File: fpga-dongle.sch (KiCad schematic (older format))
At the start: 82 parts, among them P1 right, P2 left, U1 W25Q16BVSSIG(SOIC-8_208mil), U2 SY8009AAAC(SOT23-5), U3 SY8009AAAC(SOT23-5), U4 ICE40HX1K-VQ100(VQFP100), U5 AS4C16M16S

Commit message: Assigned componets, first partial place
Signed-off-by: Martin Ribelotta <martinribelotta@gmail.com>
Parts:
- 3.3V_E1, RxD_E1, TxD_E1: footprint OLIMEX_Jumpers-FP:SJ -> OLIMEX:SJ
- BUT1, RESET1: footprint OLIMEX_Buttons-FP:T1107A(6x3,8x2,5MM) -> OLIMEX:T1107A(6x3,8x2,5MM)
- C1, C10, C2, C7, C8, C9: footprint OLIMEX_RLC-FP:C_0603_5MIL_DWS -> OLIMEX:C_0805_5MIL_DWS
- C11, C12, C13, C14, C15, C16, C17, C18, C19, C20, C21, C22, C23, C24, C25, C3, C4: footprint OLIMEX_RLC-FP:C_0402_5MIL_DWS -> OLIMEX:C_0805_5MIL_DWS
- C26, C27, C28, C29, C30, C31, C32, C33: footprint Capacitors_SMD:C_0805 -> OLIMEX:C_0805_5MIL_DWS
- C5, C6: footprint OLIMEX_RLC-FP:C_0805_5MIL_DWS -> OLIMEX:C_0805_5MIL_DWS
- CDone1, LED1, PWRLED1: footprint OLIMEX_LEDs-FP:LED_0603_KA -> LEDs:LED-0805
- CR1: footprint OLIMEX_Crystal-FP:Oscillator_7.0x5.0mm -> OLIMEX:Oscillator_7.0x5.0mm
- D1: footprint OLIMEX_Diodes-FP:DO214AA -> OLIMEX:DO214AA
- D2: footprint OLIMEX_Diodes-FP:SOD-123_1C-2A_KA -> OLIMEX:SOD-123_1C-2A_KA
- FUSE1: footprint OLIMEX_Devices-FP:FUSE-5025 -> OLIMEX:FUSE-5025
- GND1: footprint OLIMEX_Other-FP:TEST_PAD40x70_SQUARE -> OLIMEX:TEST_PAD40x70_SQUARE
- L1, L2: footprint OLIMEX_RLC-FP:CD32 -> OLIMEX:CD32
- P1, P2: footprint (none) -> Pin_Headers:Pin_Header_Straight_2x20
- P3: renamed from P?; footprint (none) -> Pin_Headers:Pin_Header_Straight_2x10
- PGM1: footprint OLIMEX_Connectors-FP:UEXT_ML10 -> OLIMEX:UEXT_ML10
- PWR1: footprint OLIMEX_Connectors-FP:PWRJ-2mm(YDJ-1136) -> OLIMEX:PWRJ-2mm(YDJ-1136)
- R1, R17, R18, R19, R2, R20, R21, R22, R23, R24, R3, R4: renamed from R?; footprint OLIMEX_RLC-FP:R_0402_5MIL_DWS -> Resistors_SMD:R_0805
- R10, R11, R12, R13, R14, R15, R16, R5, R6, R7, R8, R9: footprint OLIMEX_RLC-FP:R_0402_5MIL_DWS -> Resistors_SMD:R_0805
- U1: footprint OLIMEX_IC-FP:SO-8_208mil -> OLIMEX:SO-8_208mil
- U2, U3: footprint OLIMEX_IC-FP:SOT-23-5 -> OLIMEX:SOT-23-5
- U4: footprint OLIMEX_IC-FP:VQFP100_Pitch-0.5mm_Dimensions-16.00x16.00x1.20mm -> OLIMEX:VQFP100_Pitch-0.5mm_Dimensions-16.00x16.00x1.20mm
- U5: footprint footprints:TSOP_II_54 -> OLIMEX:SOIC-54

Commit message: First 144LQFP version. To be revised
Signed-off-by: Martin Ribelotta <martinribelotta@gmail.com>
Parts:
- removed 3.3V_E1, RxD_E1, TxD_E1: Opened, OLIMEX:SJ, symbol SJ
- removed BUT1, RESET1: T1107A(6x3,8x2,5MM), OLIMEX:T1107A(6x3,8x2,5MM), symbol T1107A(6x3,8x2,5MM)
- removed C10, C9: 22uF/6.3V/0603, OLIMEX:C_0805_5MIL_DWS, symbol C_Small
- removed C15: 100nF, OLIMEX:C_0805_5MIL_DWS, symbol C_Small
- removed C26: 100p, OLIMEX:C_0805_5MIL_DWS, symbol Csmall
- removed C27, C28, C29, C30, C31, C32, C33: 100n, OLIMEX:C_0805_5MIL_DWS, symbol Csmall
- removed D1: SMBJ6.0A, OLIMEX:DO214AA, symbol SMBJ6.0A
- removed FUSE1: NA(5025), OLIMEX:FUSE-5025, symbol FSMD035
- removed GND1: TESTPAD, OLIMEX:TEST_PAD40x70_SQUARE, symbol TESTPAD
- removed L1, L2: 2.2uH/1.5A/DCR<0.1R/CD32, OLIMEX:CD32, symbol L
- removed P3: CONN_01X20, Pin_Headers:Pin_Header_Straight_2x10, symbol CONN_01X20
- removed PGM1: BH10S, OLIMEX:UEXT_ML10, symbol BH10S
- removed PWR1: PWRJ-2mm(YDJ-1136), OLIMEX:PWRJ-2mm(YDJ-1136), symbol PWR-JAKPWR_JACK_UNI_MILLING
- removed R10: NA(22R), Resistors_SMD:R_0805, symbol R
- removed R17, R18, R19, R20, R21, R22, R23, R24: 0, Resistors_SMD:R_0805, symbol R
- removed R5, R7, R8: 4.99k/1%, Resistors_SMD:R_0805, symbol R
- removed R6: 1.1k/1%, Resistors_SMD:R_0805, symbol R
- removed U2, U3: SY8009AAAC(SOT23-5), OLIMEX:SOT-23-5, symbol SY8009AAAC(SOT23-5)
- removed U4: ICE40HX1K-VQ100(VQFP100), OLIMEX:VQFP100_Pitch-0.5mm_Dimensions-16.00x16.00x1.20mm, symbol ICE40HX1K-VQ100(VQFP100)
- added C19, C23: 100nF, OLIMEX:C_0805_5MIL_DWS, symbol C_Small
- added C25, C26, C27, C28, C29, C30, C31, C32: 100nF, symbol C_Small
- added D1: SMBJ6.0A, symbol TVS
- added F1: 1A, symbol F_Small
- added L1, L2: 2.2uH, symbol L_Small
- added P1: USB_PWR, symbol USB_OTG
- added P2: PGM, symbol CONN_02X04
- added R12: 100R, Resistors_SMD:R_0805, symbol R
- added RESET1, SW1: T1107A(6x3,8x2,5MM), symbol SW_PUSH
- added U2: sc189(Z) 3.3v, symbol sc189x
- added U3: sc189(C) 1.2v, symbol sc189x
- added U4: iCE40-HX4K-TQ144, symbol iCE40-HX4K-TQ144
- C11: value 100nF -> 10uF
- C8: renamed from C7; value 22uF/6.3V/0603 -> 10uF/6.3V/0603
- C9: renamed from C8; value 22uF/6.3V/0603 -> 10uF/6.3V/0603
- CR1: value Oscillator-100MHZ_TXC-7W -> Oscillator-50MHZ_TXC-7W
- renumbered C3 to C1, C23 to C10, C25 to C15, C1 to C2, C2 to C3, C19 to C6, C6 to C7, P1 to P3, P2 to P4, R15 to R1, R12 to R10, R13 to R11, R1 to R2, R2 to R3, R3 to R4, R4 to R5, R16 to R6, R9 to R7, R11 to R8, R14 to R9
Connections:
- net labels added: FPGA_IO_BANK1_0, FPGA_IO_BANK1_1, FPGA_IO_BANK1_10, FPGA_IO_BANK1_11, FPGA_IO_BANK1_12, FPGA_IO_BANK1_13, FPGA_IO_BANK1_14, FPGA_IO_BANK1_15, FPGA_IO_BANK1_16, FPGA_IO_BANK1_17, FPGA_IO_BANK1_18, FPGA_IO_BANK1_19, FPGA_IO_BANK1_2, FPGA_IO_BANK1_20, FPGA_IO_BANK1_21, FPGA_IO_BANK1_22, FPGA_IO_BANK1_23, FPGA_IO_BANK1_3, FPGA_IO_BANK1_4, FPGA_IO_BANK1_5, FPGA_IO_BANK1_6, FPGA_IO_BANK1_7, FPGA_IO_BANK1_8, FPGA_IO_BANK1_9, FPGA_IO_BANK2_0, FPGA_IO_BANK2_1, FPGA_IO_BANK2_10, FPGA_IO_BANK2_11, FPGA_IO_BANK2_12, FPGA_IO_BANK2_13, FPGA_IO_BANK2_14, FPGA_IO_BANK2_15, FPGA_IO_BANK2_16, FPGA_IO_BANK2_17, FPGA_IO_BANK2_18, FPGA_IO_BANK2_19, FPGA_IO_BANK2_2, FPGA_IO_BANK2_20, FPGA_IO_BANK2_21, FPGA_IO_BANK2_22, FPGA_IO_BANK2_23, FPGA_IO_BANK2_24, FPGA_IO_BANK2_25, FPGA_IO_BANK2_26, FPGA_IO_BANK2_27, FPGA_IO_BANK2_3, FPGA_IO_BANK2_4, FPGA_IO_BANK2_5, FPGA_IO_BANK2_6, FPGA_IO_BANK2_7, FPGA_IO_BANK2_8, FPGA_IO_BANK2_9, RxD, SPI_CLK, SPI_CS, TxD
- net labels removed: LCD_EN, PIO2_1, PIO2_2/I2C_SDA, PIO2_3/I2C_SCL, PIO2_4/SPI_CS, PIO2_5/SPI_MOSI, PIO2_6/SPI_MISO, PIO2_7/SPI_CLK, PIO2_8/RxD, PIO2_9/TxD, PIO3_10A, PIO3_10B, PIO3_12A, PIO3_12B, PIO3_1A, PIO3_1B, PIO3_2A, PIO3_2B, PIO3_3A, PIO3_3B, PIO3_5A, PIO3_5B, PIO3_6A, PIO3_6B, PIO3_7B, PIO3_8A, PIO3_8B
- wire segments 301 -> 195
- no-connect marks 4 -> 9
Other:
- note added: "EDU-CIAA Link"
- note added: "External IO (52 GPIO)"
- note added: "FPGA SDRAM IO and FPGA CIAA Link"
- note added: "GBIN0 as CLK"
- note added: "GBIN1 as input\nor global reset"
- note added: "L: 1.5A\nDCR<0.1R\nCD32"
- note added: "SDRAM Memory"
- note removed: "+5VDC ONLY!!!"
- note removed: "GFC was read up to the Board's part at 12.02.2016!"
- note removed: "Ra"
- note removed: "Rb"
- note removed: "Rc"
- note removed: "Rd"
- note removed: "Vout=0.6*(1+Ra/Rb)"
- note removed: "Vout=0.6*(1+Rc/Rd)"
- note removed: "When Direct SRAM programming is used, unmount R9 and populate R19!"
- moved on the sheet: C1, C10, C15, C2, C3, C4, C5, C6, C7, C8, C9, CDone1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

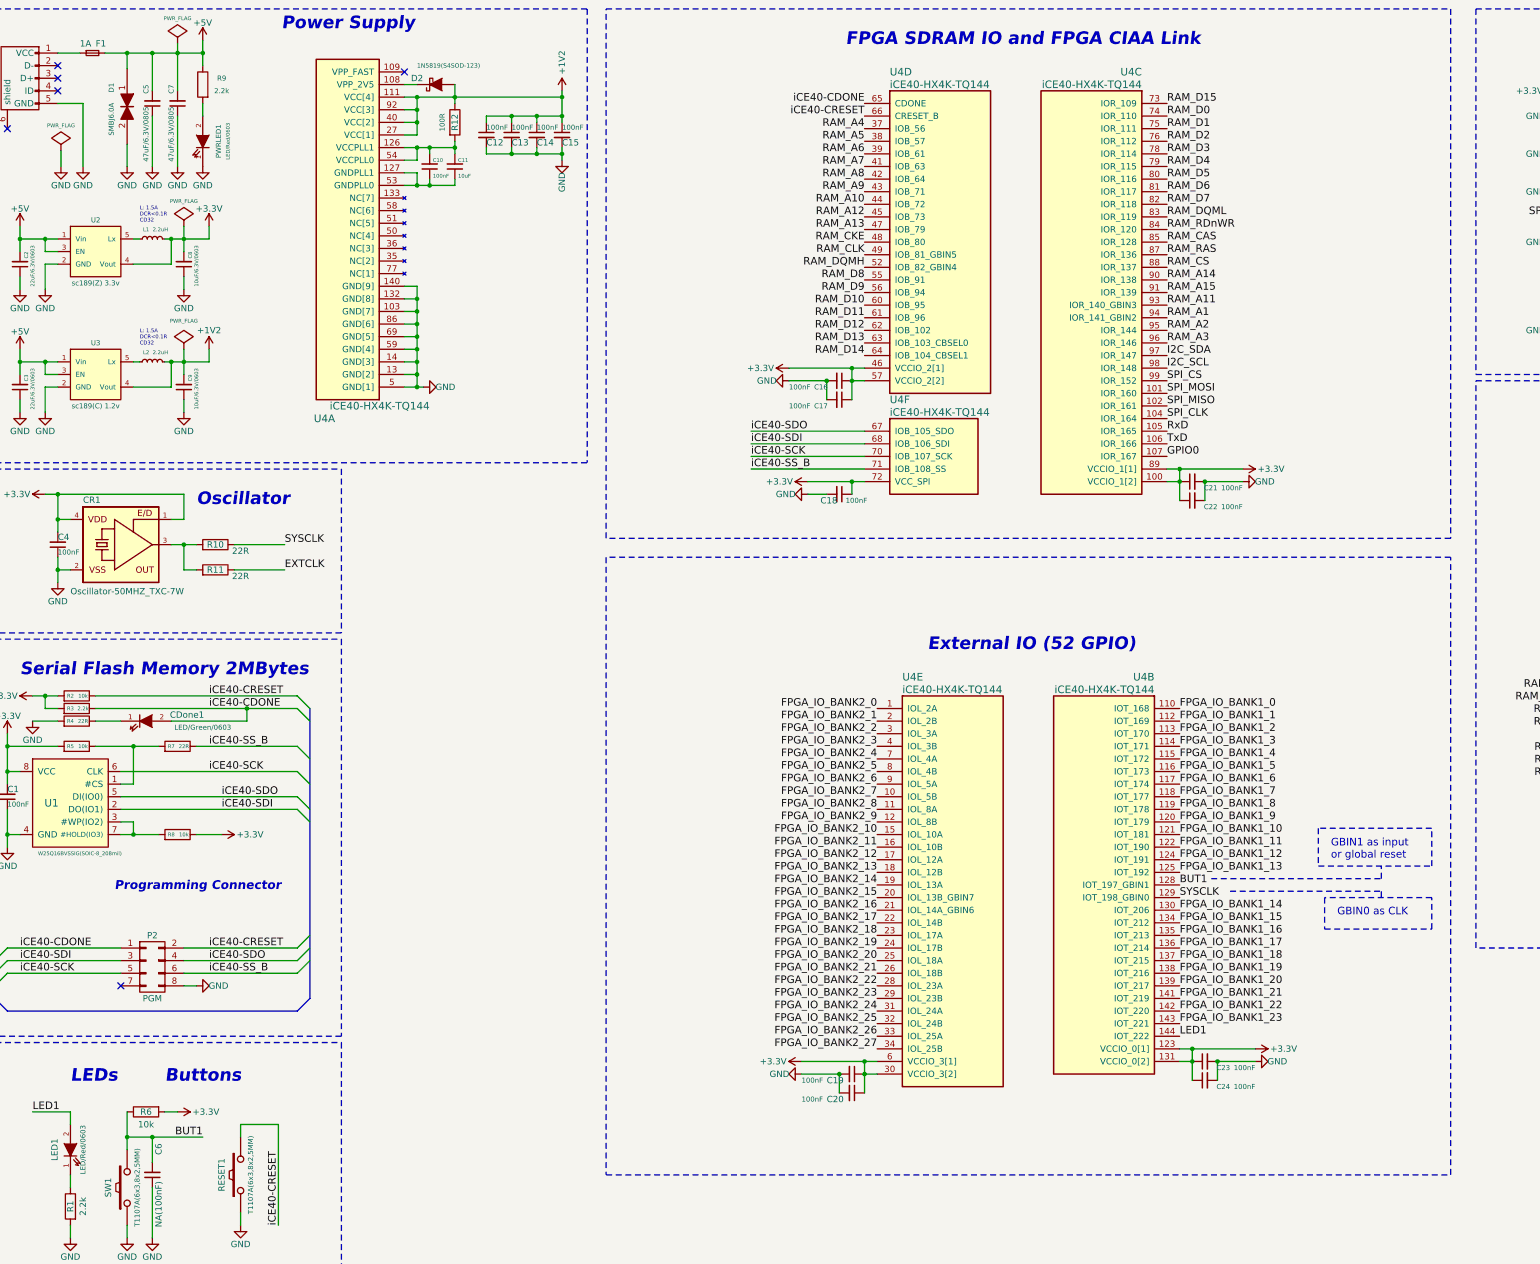
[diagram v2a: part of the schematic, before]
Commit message: First component assign and preeliminar place
Signed-off-by: Martin Ribelotta <martinribelotta@gmail.com>
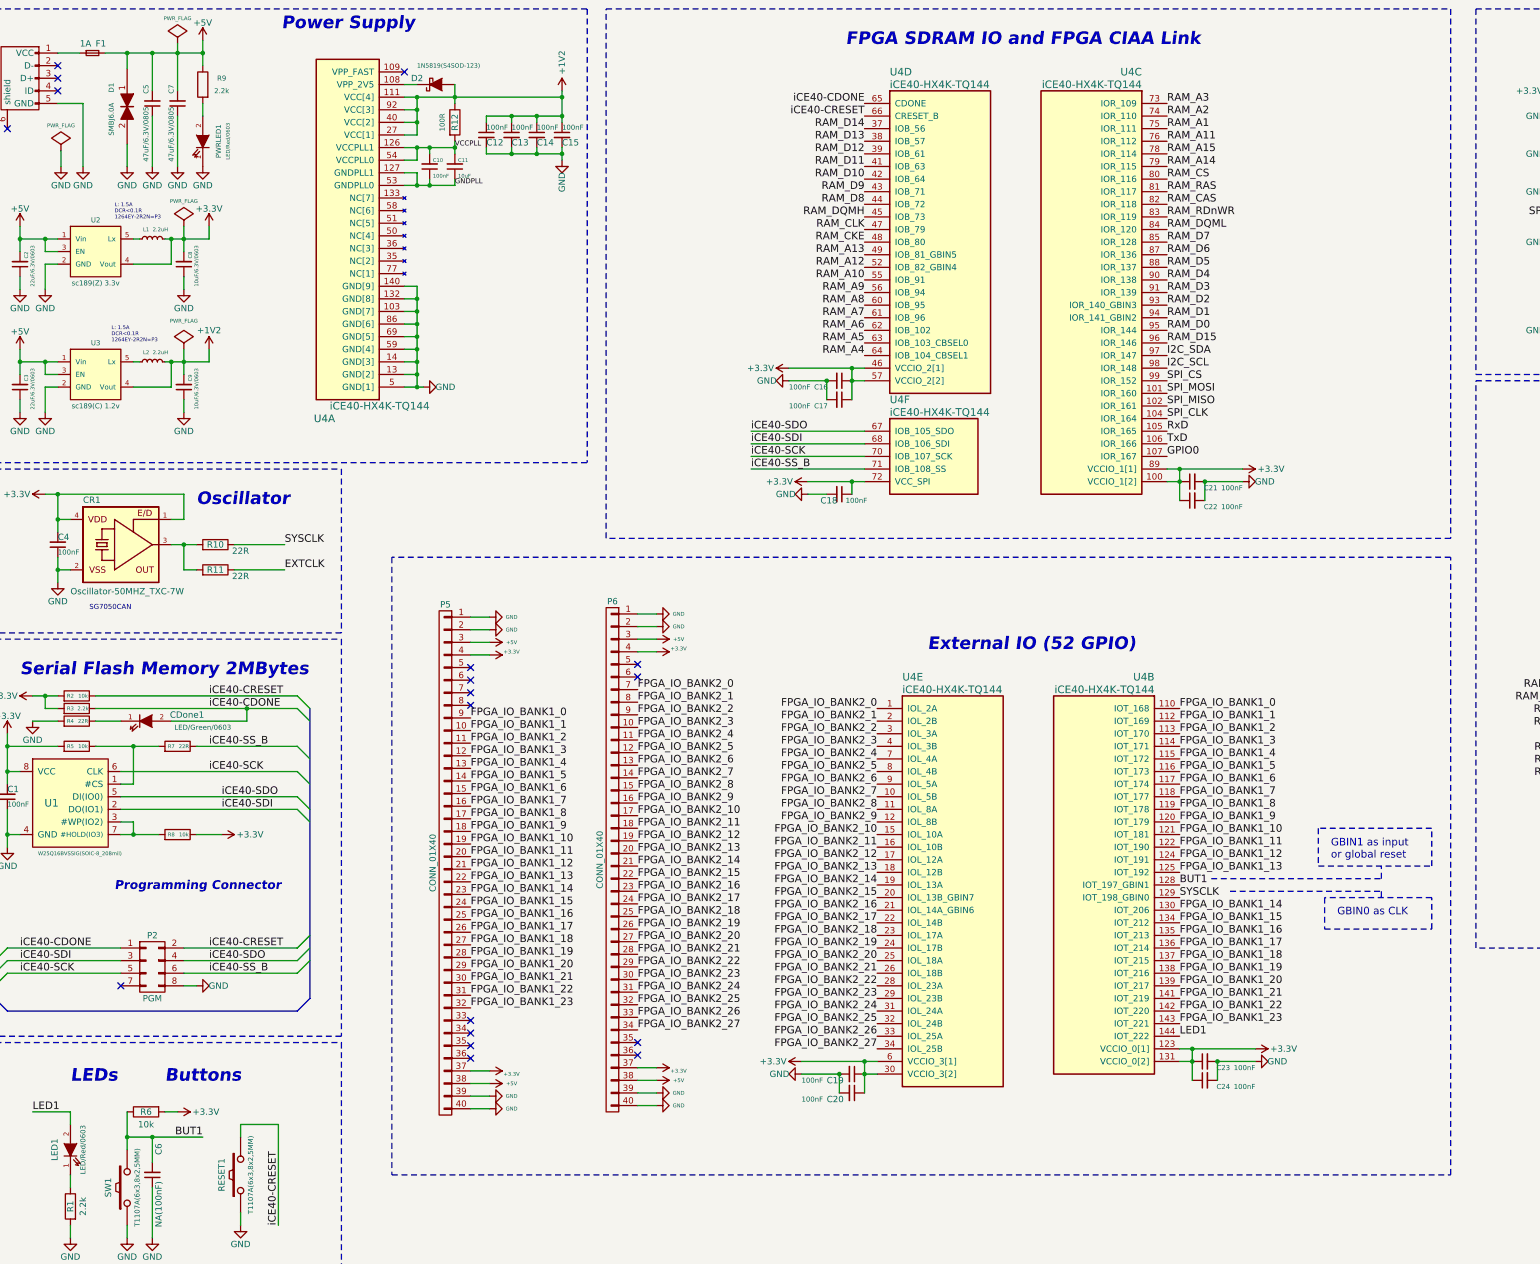
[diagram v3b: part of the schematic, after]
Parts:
- added P5, P6: CONN_01X40, Pin_Headers:Pin_Header_Straight_2x20, symbol CONN_01X40
- C1, C10, C12, C13, C14, C15, C16, C17, C18, C19, C20, C21, C22, C23, C24, C4, C6: footprint OLIMEX:C_0805_5MIL_DWS -> Capacitors_SMD:C_0805
- C11, C2, C3, C5, C7, C8, C9: footprint OLIMEX:C_0805_5MIL_DWS -> Capacitors_SMD:C_1206
- C25, C26, C27, C28, C29, C30, C31, C32: footprint (none) -> Capacitors_SMD:C_0805
- CR1: footprint OLIMEX:Oscillator_7.0x5.0mm -> OLIMEX_Crystal-FP:Oscillator_7.0x5.0mm
- D1: footprint (none) -> Diodes_SMD:DO-214AB
- D2: footprint OLIMEX:SOD-123_1C-2A_KA -> Diodes_SMD:SOD-123
- F1: footprint (none) -> OLIMEX_Devices-FP:FUSE-1206
- L1, L2: footprint (none) -> Choke_SMD:Choke_SMD_6.3x6.3_H3
- P1: footprint (none) -> OLIMEX_Connectors-FP:USB_Mini-B-NOSILK
- P2: footprint (none) -> Pin_Headers:Pin_Header_Straight_2x04
- RESET1, SW1: footprint (none) -> Buttons_Switches_SMD:SW_SPST_PTS645
- U1: footprint OLIMEX:SO-8_208mil -> OLIMEX_IC-FP:SOIC-8_208mil
- U2, U3: footprint (none) -> OLIMEX_Regulators-FP:SOT-23-5
- U4: footprint (none) -> Housings_QFP:LQFP-144_20x20mm_Pitch0.5mm
- U5: footprint OLIMEX:SOIC-54 -> mribelotta:TSOP_II_54
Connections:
- net +3V3: now also P5.37 (P37), P5.4 (P4), P6.37 (P37), P6.4 (P4)
- net +5V: now also P5.3 (P3), P5.38 (P38), P6.3 (P3), P6.38 (P38)
- net FPGA_IO_BANK1_0: now also P5.9 (P9)
- net FPGA_IO_BANK1_1: now also P5.10 (P10)
- net FPGA_IO_BANK1_10: now also P5.19 (P19)
- net FPGA_IO_BANK1_11: now also P5.20 (P20)
- net FPGA_IO_BANK1_12: now also P5.21 (P21)
- net FPGA_IO_BANK1_13: now also P5.22 (P22)
- net FPGA_IO_BANK1_14: now also P5.23 (P23)
- net FPGA_IO_BANK1_15: now also P5.24 (P24)
- net FPGA_IO_BANK1_16: now also P5.25 (P25)
- net FPGA_IO_BANK1_17: now also P5.26 (P26)
- net FPGA_IO_BANK1_18: now also P5.27 (P27)
- net FPGA_IO_BANK1_19: now also P5.28 (P28)
- net FPGA_IO_BANK1_2: now also P5.11 (P11)
- net FPGA_IO_BANK1_20: now also P5.29 (P29)
- net FPGA_IO_BANK1_21: now also P5.30 (P30)
- net FPGA_IO_BANK1_22: now also P5.31 (P31)
- net FPGA_IO_BANK1_23: now also P5.32 (P32)
- net FPGA_IO_BANK1_3: now also P5.12 (P12)
- net FPGA_IO_BANK1_4: now also P5.13 (P13)
- net FPGA_IO_BANK1_5: now also P5.14 (P14)
- net FPGA_IO_BANK1_6: now also P5.15 (P15)
- net FPGA_IO_BANK1_7: now also P5.16 (P16)
- net FPGA_IO_BANK1_8: now also P5.17 (P17)
- net FPGA_IO_BANK1_9: now also P5.18 (P18)
- net FPGA_IO_BANK2_0: now also P6.7 (P7)
- net FPGA_IO_BANK2_1: now also P6.8 (P8)
- net FPGA_IO_BANK2_10: now also P6.17 (P17)
- net FPGA_IO_BANK2_11: now also P6.18 (P18)
- net FPGA_IO_BANK2_12: now also P6.19 (P19)
- net FPGA_IO_BANK2_13: now also P6.20 (P20)
- net FPGA_IO_BANK2_14: now also P6.21 (P21)
- net FPGA_IO_BANK2_15: now also P6.22 (P22)
- net FPGA_IO_BANK2_16: now also P6.23 (P23)
- net FPGA_IO_BANK2_17: now also P6.24 (P24)
- net FPGA_IO_BANK2_18: now also P6.25 (P25)
- net FPGA_IO_BANK2_19: now also P6.26 (P26)
- net FPGA_IO_BANK2_2: now also P6.9 (P9)
- net FPGA_IO_BANK2_20: now also P6.27 (P27)
- net FPGA_IO_BANK2_21: now also P6.28 (P28)
- net FPGA_IO_BANK2_22: now also P6.29 (P29)
- net FPGA_IO_BANK2_23: now also P6.30 (P30)
- net FPGA_IO_BANK2_24: now also P6.31 (P31)
- net FPGA_IO_BANK2_25: now also P6.32 (P32)
- net FPGA_IO_BANK2_26: now also P6.33 (P33)
- net FPGA_IO_BANK2_27: now also P6.34 (P34)
- net FPGA_IO_BANK2_3: now also P6.10 (P10)
- net FPGA_IO_BANK2_4: now also P6.11 (P11)
- net FPGA_IO_BANK2_5: now also P6.12 (P12)
- net FPGA_IO_BANK2_6: now also P6.13 (P13)
- net FPGA_IO_BANK2_7: now also P6.14 (P14)
- net FPGA_IO_BANK2_8: now also P6.15 (P15)
- net FPGA_IO_BANK2_9: now also P6.16 (P16)
- net GND: now also P5.1 (P1), P5.2 (P2), P5.39 (P39), P5.40 (P40), P6.1 (P1), P6.2 (P2), P6.39 (P39), P6.40 (P40)
- net RAM_A1: now also U4.75 (IOR_111); no longer U4.94 (IOR_141_GBIN2)
- net RAM_A10: now also U4.55 (IOB_91); no longer U4.44 (IOB_72)
- net RAM_A11: now also U4.76 (IOR_112); no longer U4.93 (IOR_140_GBIN3)
- net RAM_A12: now also U4.52 (IOB_82_GBIN4); no longer U4.45 (IOB_73)
- net RAM_A13: now also U4.49 (IOB_81_GBIN5); no longer U4.47 (IOB_79)
- net RAM_A14: now also U4.79 (IOR_115); no longer U4.90 (IOR_138)
- net RAM_A15: now also U4.78 (IOR_114); no longer U4.91 (IOR_139)
- net RAM_A2: now also U4.74 (IOR_110); no longer U4.95 (IOR_144)
- net RAM_A3: now also U4.73 (IOR_109); no longer U4.96 (IOR_146)
- net RAM_A4: now also U4.64 (IOB_104_CBSEL1); no longer U4.37 (IOB_56)
- net RAM_A5: now also U4.63 (IOB_103_CBSEL0); no longer U4.38 (IOB_57)
- net RAM_A6: now also U4.62 (IOB_102); no longer U4.39 (IOB_61)
- net RAM_A7: now also U4.61 (IOB_96); no longer U4.41 (IOB_63)
- net RAM_A8: now also U4.60 (IOB_95); no longer U4.42 (IOB_64)
- net RAM_A9: now also U4.56 (IOB_94); no longer U4.43 (IOB_71)
- net RAM_CAS: now also U4.82 (IOR_118); no longer U4.85 (IOR_128)
- net RAM_CLK: now also U4.47 (IOB_79); no longer U4.49 (IOB_81_GBIN5)
- net RAM_CS: now also U4.80 (IOR_116); no longer U4.88 (IOR_137)
- net RAM_D0: now also U4.95 (IOR_144); no longer U4.74 (IOR_110)
- net RAM_D1: now also U4.94 (IOR_141_GBIN2); no longer U4.75 (IOR_111)
- net RAM_D10: now also U4.42 (IOB_64); no longer U4.60 (IOB_95)
- net RAM_D11: now also U4.41 (IOB_63); no longer U4.61 (IOB_96)
- net RAM_D12: now also U4.39 (IOB_61); no longer U4.62 (IOB_102)
- net RAM_D13: now also U4.38 (IOB_57); no longer U4.63 (IOB_103_CBSEL0)
- net RAM_D14: now also U4.37 (IOB_56); no longer U4.64 (IOB_104_CBSEL1)
- net RAM_D15: now also U4.96 (IOR_146); no longer U4.73 (IOR_109)
- net RAM_D2: now also U4.93 (IOR_140_GBIN3); no longer U4.76 (IOR_112)
- net RAM_D3: now also U4.91 (IOR_139); no longer U4.78 (IOR_114)
- net RAM_D4: now also U4.90 (IOR_138); no longer U4.79 (IOR_115)
- net RAM_D5: now also U4.88 (IOR_137); no longer U4.80 (IOR_116)
- net RAM_D6: now also U4.87 (IOR_136); no longer U4.81 (IOR_117)
- net RAM_D7: now also U4.85 (IOR_128); no longer U4.82 (IOR_118)
- net RAM_D8: now also U4.44 (IOB_72); no longer U4.55 (IOB_91)
- net RAM_D9: now also U4.43 (IOB_71); no longer U4.56 (IOB_94)
- net RAM_DQMH: now also U4.45 (IOB_73); no longer U4.52 (IOB_82_GBIN4)
- net RAM_DQML: now also U4.84 (IOR_120); no longer U4.83 (IOR_119)
- net RAM_RAS: now also U4.81 (IOR_117); no longer U4.87 (IOR_136)
- net RAM_RDnWR: now also U4.83 (IOR_119); no longer U4.84 (IOR_120)
- net GNDPLL: now reaches C10.1, C11.1, U4.127 (GNDPLL1), U4.53 (GNDPLL0)
- net VCCPLL: now reaches C10.2, C11.2, R12.2, U4.126 (VCCPLL1), U4.54 (VCCPLL0)
- no-connect marks 9 -> 21
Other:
- note added: "L: 1.5A\nDCR<0.1R\n1264EY-2R2N=P3"
- note added: "SG7050CAN"
- note removed: "L: 1.5A\nDCR<0.1R\nCD32"
